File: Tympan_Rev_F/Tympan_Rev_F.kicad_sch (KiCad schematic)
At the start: 91 parts, among them J1 SJ-3523-SMT-TR, J2 SJ-3524-SMT-TR-PI, J3 Conn_01x06, J4 Qwiik Connector, J7 J-Link, P1 CONN_01X06, P2 CONN_01X06, P3 CONN_01X06, P4 CONN_01X06, P6 CONN_01X01, P7 CONN_01X01, P8 CONN_01X01, SW1 CL-SB-22A, SW2 SW_Push, U1 MCP73831, U2 TLV320AIC3206IRSBT, U3 74LVC1G66, U4 LP5907MFX-1.8, U5 Teensy4.1, U6 LC709203, U7 MDBT50Q-1MV2, Y1 32.768

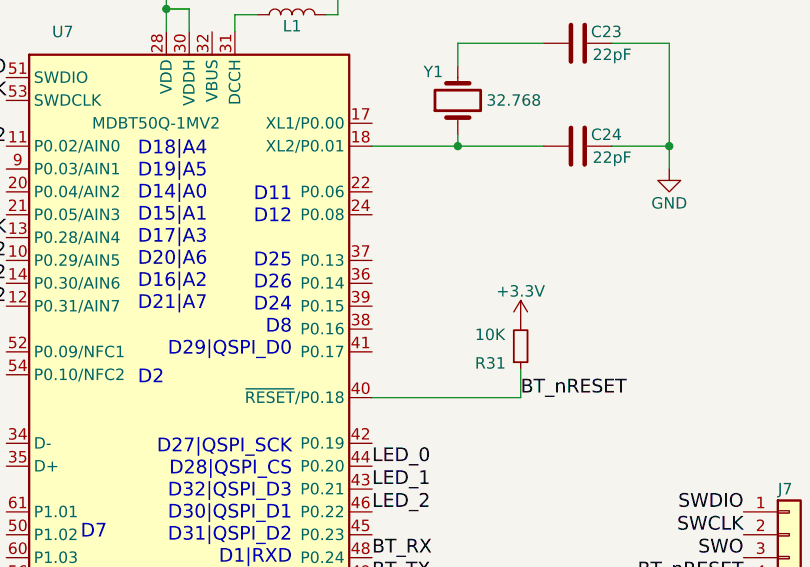
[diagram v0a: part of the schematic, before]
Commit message: Added SPI
Selected pins to bring SPI connection to the BLE moudule
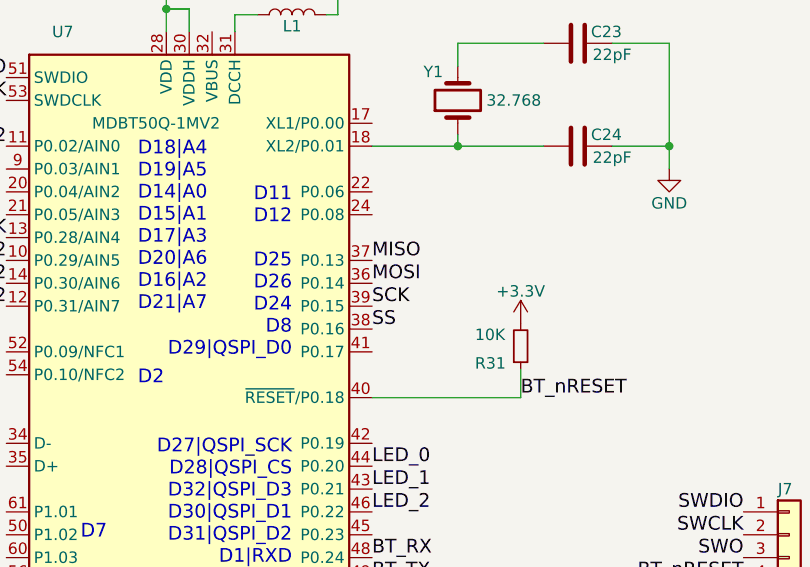
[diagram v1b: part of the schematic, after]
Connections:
- net MISO: now also U7.37 (P0.13)
- net MOSI: now also U7.36 (P0.14)
- net SCK: now also U7.39 (P0.15)
- net SS: now also U7.38 (P0.16)
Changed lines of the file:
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@@
     (effects (font (size 1.524 1.524)) (justify right bottom))
+  )
+  (label "SS" (at 137.795 311.785 0) (fields_autoplaced)
+    (effects (font (size 1.524 1.524)) (justify left bottom))
   )
   (label "BCLK" (at 97.155 301.625 180) (fields_autoplaced)
@@
     (effects (font (size 1.524 1.524)) (justify right bottom))
   )
+  (label "MISO" (at 137.795 304.165 0) (fields_autoplaced)
+    (effects (font (size 1.524 1.524)) (justify left bottom))
+  )
   (label "BT_nRESET" (at 154.305 319.405 0) (fields_autoplaced)
     (effects (font (size 1.524 1.524)) (justify left bottom))
@@
   )
   (label "BT_PIO0" (at 202.565 276.225 0) (fields_autoplaced)
+    (effects (font (size 1.524 1.524)) (justify left bottom))
+  )
+  (label "SCK" (at 137.795 309.245 0) (fields_autoplaced)
     (effects (font (size 1.524 1.524)) (justify left bottom))
   )
@@
     (effects (font (size 1.524 1.524)) (justify left bottom))
   )
+  (label "MOSI" (at 137.795 306.705 0) (fields_autoplaced)
+    (effects (font (size 1.524 1.524)) (justify left bottom))
+  )

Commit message: Added pdf of schematic
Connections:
- net LED_A is gone; now on net LED_G: U5.37 (15_A1_RX3_SPDIF_IN)
- net BT_CS: now reaches U5.30 (38_CS1_IN1)
- net BT_CS: now also U7.38 (P0.16)
- net SS renamed CS
- net CS: no longer U7.38 (P0.16)
- net VREGEN: no longer names the net of U5.36 (14_A0_TX3_SPDIF_OUT)
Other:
- title: Tympan Rev E -> Tympan Rev F
- moved on the sheet: R21, R25
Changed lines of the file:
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@@
   (paper "C")
   (title_block
-    (title "Tympan Rev E")
-    (date "2021-04-26")
-    (rev "v2")
+    (title "Tympan Rev F")
+    (date "2024-01-19")
+    (rev "v1")
     (company "Tympan Master Hearing Aid Project")
     (comment 1 "Designed by Flywheel Lab, Brooklyn")
@@
     (effects (font (size 1.524 1.524)) (justify right bottom))
   )
-  (text "Possible trash?" (at 361.95 52.705 0)
-    (effects (font (size 1.524 1.524)) (justify left bottom))
-  )
   (text "3352T-1-103L" (at 455.93 219.075 90)
     (effects (font (size 1.524 1.524) (thickness 0.3048) bold) (justify left bottom))
@@
     (effects (font (size 1.524 1.524) (thickness 0.3048) bold) (justify left bottom))
   )
-  (text "Possible trash?" (at 200.025 278.765 0)
+  (text "Possible trash?" (at 170.18 374.65 0)
     (effects (font (size 1.524 1.524)) (justify left bottom))
   )
@@
     (effects (font (size 1.524 1.524)) (justify right bottom))
   )
-  (label "BT_PIO0" (at 373.38 50.165 180) (fields_autoplaced)
-    (effects (font (size 1.524 1.524)) (justify right bottom))
-  )
   (label "SCK" (at 318.77 316.23 180) (fields_autoplaced)
     (effects (font (size 1.524 1.524)) (justify right bottom))
@@
     (effects (font (size 1.524 1.524)) (justify left bottom))
   )
-  (label "BT_PIO5" (at 373.38 46.99 180) (fields_autoplaced)
-    (effects (font (size 1.524 1.524)) (justify right bottom))
-  )
   (label "LOL" (at 143.51 191.77 180) (fields_autoplaced)
     (effects (font (size 1.524 1.524)) (justify right bottom))
@@
     (effects (font (size 1.524 1.524)) (justify left bottom))
   )
-  (label "BT_PIO5" (at 202.565 273.685 0) (fields_autoplaced)
-    (effects (font (size 1.524 1.524)) (justify left bottom))
-  )
-  (label "SS" (at 394.335 85.725 180) (fields_autoplaced)
+  (label "CS" (at 394.335 85.725 180) (fields_autoplaced)
     (effects (font (size 1.524 1.524)) (justify right bottom))
   )
@@
     (effects (font (size 1.524 1.524)) (justify right bottom))
   )
-  (label "SS" (at 318.77 318.77 180) (fields_autoplaced)
+  (label "CS" (at 318.77 318.77 180) (fields_autoplaced)
     (effects (font (size 1.524 1.524)) (justify right bottom))
   )
@@
     (effects (font (size 1.524 1.524)) (justify right bottom))
   )
-  (label "LED_A" (at 450.215 85.725 0) (fields_autoplaced)
+  (label "LED_G" (at 450.215 85.725 0) (fields_autoplaced)
     (effects (font (size 1.524 1.524)) (justify left bottom))
   )
@@
     (effects (font (size 1.524 1.524)) (justify left bottom))
   )
-  (label "VREGEN" (at 450.215 88.265 0) (fields_autoplaced)
-    (effects (font (size 1.524 1.524)) (justify left bottom))
-  )
   (label "DOUT_1" (at 337.82 308.61 0) (fields_autoplaced)
     (effects (font (size 1.524 1.524)) (justify left bottom))
@@
     (effects (font (size 1.524 1.524)) (justify right bottom))
   )
-  (label "SS" (at 137.795 311.785 0) (fields_autoplaced)
+  (label "BT_CS" (at 137.795 311.785 0) (fields_autoplaced)
     (effects (font (size 1.524 1.524)) (justify left bottom))
   )
@@
     (effects (font (size 1.524 1.524)) (justify left bottom))
   )
+  (label "BT_CS" (at 450.215 103.505 0) (fields_autoplaced)
+    (effects (font (size 1.524 1.524)) (justify left bottom))
+  )
   (label "IN2_R" (at 143.51 184.15 180) (fields_autoplaced)
     (effects (font (size 1.524 1.524)) (justify right bottom))
@@
     (effects (font (size 1.524 1.524)) (justify right bottom))
   )
-  (label "BT_PIO0" (at 202.565 276.225 0) (fields_autoplaced)
-    (effects (font (size 1.524 1.524)) (justify left bottom))
-  )
   (label "SCK" (at 137.795 309.245 0) (fields_autoplaced)
     (effects (font (size 1.524 1.524)) (justify left bottom))
@@
     )
   )
-  (symbol (lib_id "Device:R_Small") (at 203.2 266.065 0) (unit 1)
+  (symbol (lib_id "Device:R_Small") (at 174.625 367.03 0) (unit 1)
     (in_bom yes) (on_board yes) (dnp no)
-    (property "Reference" "R21" (at 203.962 265.557 0)
+    (property "Reference" "R21" (at 175.387 366.522 0)
       (effects (font (size 1.27 1.27)) (justify left))
     )
-    (property "Value" "1K" (at 203.962 267.081 0)
+    (property "Value" "1K" (at 175.387 368.046 0)
       (effects (font (size 1.27 1.27)) (justify left))
     )
-    (property "Footprint" "Resistor_SMD:R_0402_1005Metric" (at 203.2 266.065 0)
+    (property "Footprint" "Resistor_SMD:R_0402_1005Metric" (at 174.625 367.03 0)
       (effects (font (size 1.27 1.27)) hide)
     )
-    (property "Datasheet" "" (at 203.2 266.065 0)
+    (property "Datasheet" "" (at 174.625 367.03 0)
       (effects (font (size 1.27 1.27)))
     )
@@
     )
   )
-  (symbol (lib_id "Device:R_Small") (at 209.55 266.7 180) (unit 1)
+  (symbol (lib_id "Device:R_Small") (at 180.975 367.665 180) (unit 1)
     (in_bom yes) (on_board yes) (dnp no)
-    (property "Reference" "R25" (at 214.63 267.335 0)
+    (property "Reference" "R25" (at 186.055 368.3 0)
       (effects (font (size 1.27 1.27)) (justify left))
     )
-    (property "Value" "100K" (at 215.9 265.43 0)
+    (property "Value" "100K" (at 187.325 366.395 0)
       (effects (font (size 1.27 1.27)) (justify left))
     )
-    (property "Footprint" "Resistor_SMD:R_0402_1005Metric" (at 209.55 266.7 0)
+    (property "Footprint" "Resistor_SMD:R_0402_1005Metric" (at 180.975 367.665 0)
       (effects (font (size 1.27 1.27)) hide)
     )
-    (property "Datasheet" "" (at 209.55 266.7 0)
+    (property "Datasheet" "" (at 180.975 367.665 0)
       (effects (font (size 1.27 1.27)))
     )

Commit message: Swapped the SPI bus
moved nRESET pin to open up SPI_1 pins for exclusive connection to the BT module.
This frees up our existing SPI bus breakout for use as SPI or as GPIO
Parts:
- removed R21: 1K, Resistor_SMD:R_0402_1005Metric, symbol Device:R_Small
- removed R25: 100K, Resistor_SMD:R_0402_1005Metric, symbol Device:R_Small
- R26, R27, R28: value 470R -> 1K
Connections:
- net MISO: no longer U7.37 (P0.13)
- net MOSI: no longer U7.36 (P0.14)
- net SCK: no longer U7.39 (P0.15)
- net nRESET: now also U5.32 (40_A16); no longer U5.18 (26_A12_MOSI1)
- net SCK1: now reaches U5.19 (27_A13_SCK1)
- net SCK1: now also U7.39 (P0.15)
- net MISO1: now reaches U5.31 (39_MISO1_OUT1A)
- net MISO1: now also U7.37 (P0.13)
- new net MOSI1: U5.18 (26_A12_MOSI1), U7.36 (P0.14)
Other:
- note removed: "Possible trash?"
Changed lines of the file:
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@@
     (effects (font (size 1.524 1.524) (thickness 0.3048) bold) (justify left bottom))
   )
-  (text "Possible trash?" (at 170.18 374.65 0)
-    (effects (font (size 1.524 1.524)) (justify left bottom))
-  )
   (text "I2C ADDRESS 0011000" (at 95.25 191.77 0)
     (effects (font (size 1.524 1.524)) (justify left bottom))
@@
     (effects (font (size 1.524 1.524)) (justify left bottom))
   )
+  (label "MOSI1" (at 394.335 100.965 180) (fields_autoplaced)
+    (effects (font (size 1.524 1.524)) (justify right bottom))
+  )
   (label "IN1_L" (at 250.19 309.88 180) (fields_autoplaced)
     (effects (font (size 1.524 1.524)) (justify right bottom))
@@
     (effects (font (size 1.524 1.524)) (justify left bottom))
   )
+  (label "MISO1" (at 450.215 100.965 0) (fields_autoplaced)
+    (effects (font (size 1.524 1.524)) (justify left bottom))
+  )
+  (label "SCK1" (at 394.335 103.505 180) (fields_autoplaced)
+    (effects (font (size 1.524 1.524)) (justify right bottom))
+  )
   (label "DOUT_1" (at 337.82 308.61 0) (fields_autoplaced)
     (effects (font (size 1.524 1.524)) (justify left bottom))
@@
     (effects (font (size 1.524 1.524)) (justify right bottom))
   )
-  (label "MISO" (at 137.795 304.165 0) (fields_autoplaced)
+  (label "MISO1" (at 137.795 304.165 0) (fields_autoplaced)
     (effects (font (size 1.524 1.524)) (justify left bottom))
   )
@@
     (effects (font (size 1.524 1.524)) (justify right bottom))
   )
-  (label "SCK" (at 137.795 309.245 0) (fields_autoplaced)
+  (label "SCK1" (at 137.795 309.245 0) (fields_autoplaced)
     (effects (font (size 1.524 1.524)) (justify left bottom))
   )
@@
     (effects (font (size 1.524 1.524)) (justify left bottom))
   )
-  (label "nRESET" (at 394.335 100.965 180) (fields_autoplaced)
-    (effects (font (size 1.524 1.524)) (justify right bottom))
+  (label "nRESET" (at 450.215 98.425 0) (fields_autoplaced)
+    (effects (font (size 1.524 1.524)) (justify left bottom))
   )
   (label "LED_G" (at 443.23 193.675 0) (fields_autoplaced)
@@
     (effects (font (size 1.524 1.524)) (justify left bottom))
   )
-  (label "MOSI" (at 137.795 306.705 0) (fields_autoplaced)
+  (label "MOSI1" (at 137.795 306.705 0) (fields_autoplaced)
     (effects (font (size 1.524 1.524)) (justify left bottom))
   )
@@
     )
   )
-  (symbol (lib_id "Device:R_Small") (at 174.625 367.03 0) (unit 1)
-    (in_bom yes) (on_board yes) (dnp no)
-    (property "Reference" "R21" (at 175.387 366.522 0)
-      (effects (font (size 1.27 1.27)) (justify left))
-    )
-    (property "Value" "1K" (at 175.387 368.046 0)
-      (effects (font (size 1.27 1.27)) (justify left))
-    )
-    (property "Footprint" "Resistor_SMD:R_0402_1005Metric" (at 174.625 367.03 0)
-      (effects (font (size 1.27 1.27)) hide)
-    )
-    (property "Datasheet" "" (at 174.625 367.03 0)
-      (effects (font (size 1.27 1.27)))
-    )
-    (pin "1")
-    (pin "2")
-    (instances
-      (project "Tympan_Rev_F"
-        (path "/0895d2a9-2102-4837-8faf-68ca65e88f0b"
-          (reference "R21") (unit 1)
-        )
-      )
-    )
-  )
-  (symbol (lib_id "Device:R_Small") (at 180.975 367.665 180) (unit 1)
-    (in_bom yes) (on_board yes) (dnp no)
-    (property "Reference" "R25" (at 186.055 368.3 0)
-      (effects (font (size 1.27 1.27)) (justify left))
-    )
-    (property "Value" "100K" (at 187.325 366.395 0)
-      (effects (font (size 1.27 1.27)) (justify left))
-    )
-    (property "Footprint" "Resistor_SMD:R_0402_1005Metric" (at 180.975 367.665 0)
-      (effects (font (size 1.27 1.27)) hide)
-    )
-    (property "Datasheet" "" (at 180.975 367.665 0)
-      (effects (font (size 1.27 1.27)))
-    )
-    (pin "1")
-    (pin "2")
-    (instances
-      (project "Tympan_Rev_F"
-        (path "/0895d2a9-2102-4837-8faf-68ca65e88f0b"
-          (reference "R25") (unit 1)
-        )
-      )
-    )
-  )
   (symbol (lib_id "power:GND") (at 67.945 287.02 0) (unit 1)
     (in_bom yes) (on_board yes) (dnp no)
@@
       (effects (font (size 1.27 1.27)) (justify left))
     )
-    (property "Value" "470R" (at 64.135 354.33 90)
+    (property "Value" "1K" (at 64.135 354.33 90)
       (effects (font (size 1.27 1.27)) (justify left))
     )
@@
       (effects (font (size 1.27 1.27)) (justify left))
     )
-    (property "Value" "470R" (at 64.135 360.68 90)
+    (property "Value" "1K" (at 64.135 360.68 90)
       (effects (font (size 1.27 1.27)) (justify left))
     )
@@
       (effects (font (size 1.27 1.27)) (justify left))
     )
-    (property "Value" "470R" (at 64.135 367.03 90)
+    (property "Value" "1K" (at 64.135 367.03 90)
       (effects (font (size 1.27 1.27)) (justify left))
     )
@@
   (symbol (lib_id "Device:R_Small") (at 381.635 95.885 270) (mirror x) (unit 1)
     (in_bom yes) (on_board yes) (dnp no)
-    (property "Reference" "R32" (at 380.365 95.885 90)
+    (property "Reference" "R32" (at 377.825 93.98 90)
       (effects (font (size 1.27 1.27)) (justify left))
     )
-    (property "Value" "4K7" (at 380.365 93.345 90)
+    (property "Value" "4K7" (at 382.27 93.98 90)
       (effects (font (size 1.27 1.27)) (justify left))
     )
@@
   (symbol (lib_id "Device:R_Small") (at 381.635 98.425 270) (mirror x) (unit 1)
     (in_bom yes) (on_board yes) (dnp no)
-    (property "Reference" "R33" (at 380.365 98.425 90)
+    (property "Reference" "R33" (at 376.555 100.965 90)
       (effects (font (size 1.27 1.27)) (justify left))
     )
-    (property "Value" "4K7" (at 379.095 100.965 90)
+    (property "Value" "4K7" (at 381 100.965 90)
       (effects (font (size 1.27 1.27)) (justify left))
     )
